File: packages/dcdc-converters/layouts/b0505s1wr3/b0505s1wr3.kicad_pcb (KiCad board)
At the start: 2 copper layers, 7 parts

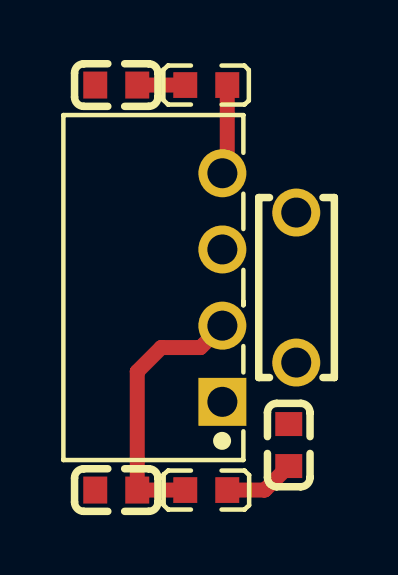
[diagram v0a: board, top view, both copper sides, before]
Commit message: Convert B0505 into ato
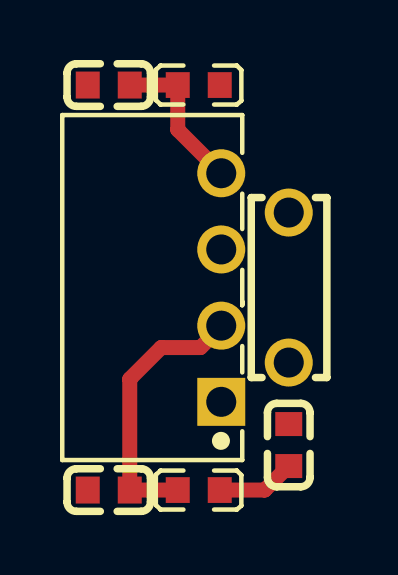
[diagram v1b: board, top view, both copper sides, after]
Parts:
- C2, C3: value 4.7µF ±10% 10V X5R -> 4.7nF ±10% 50V X7R
- moved C2 6.18 mm to (-1.50, 6.75), turned to 180 degrees
- moved C3 5.94 mm to (4.50, 5.25), turned to 90 degrees
- moved C1 0.25 mm to (4.50, 0.00)
- moved C4 0.25 mm to (-1.50, -6.75)
- moved L1 0.25 mm to (1.50, 6.75), turned to 0 degrees
- moved L2 0.25 mm to (1.50, -6.75)
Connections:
- C2 pad 1: hv -> plusVin
- C3 pad 1: hv-2 -> hv-1
- C4 pad 1: hv-1 -> plusVout
- L1 pad 1: hv -> plusVin
- L1 pad 2: hv-2 -> hv-1
- L2 pad 1: hv-1 -> plusVout
- L2 pad 2: hv-3 -> hv
- U1 pad 2: hv-2 -> plusVin
- U1 pad 4: hv-3 -> plusVout
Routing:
- net plusVin: track 0.00 -> 9.12 mm
- net hv-2: track 9.02 -> 0.00 mm
- net plusVout: track 0.00 -> 5.14 mm
- net hv-3: track 3.01 -> 0.00 mm
- net hv: track 2.38 -> 0.00 mm
- net hv-1: track 1.60 -> 2.63 mm

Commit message: Rebuild all
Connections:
- C3 pad 1: hv-1 -> hv
- L1 pad 2: hv-1 -> hv
- L2 pad 2: hv -> hv-1
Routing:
- net hv-1: track 2.63 -> 0.00 mm
- net hv: track 0.00 -> 2.63 mm
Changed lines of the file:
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@@
     )
     (net 0 "")
-    (net 1 "hv")
+    (net 1 "hv-1")
     (net 2 "plusVout")
     (net 3 "plusVin")
-    (net 4 "hv-1")
+    (net 4 "hv")
     (net 5 "gnd")
     (net 6 "gnd-1")
@@
             (size 0.8 0.86)
             (layers "F.Cu" "F.Mask" "F.Paste")
-            (net 4 "hv-1")
+            (net 4 "hv")
         )
         (embedded_fonts no)
@@
             (size 0.8 0.86)
             (layers "F.Cu" "F.Mask" "F.Paste")
-            (net 1 "hv")
+            (net 1 "hv-1")
         )
         (embedded_fonts no)
@@
             (size 0.8 0.9)
             (layers "F.Cu" "F.Mask" "F.Paste")
-            (net 4 "hv-1")
+            (net 4 "hv")
         )
         (pad "2" smd rect

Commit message: Update packages to ato v0.9.x (#36)
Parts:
- C1: footprint atopile:CAP-TH_L6.0-W2.5-P5.00-D1.0-5e41da -> STE_R06B1B271KN0B0S0N0:CAP-TH_L6.0-W2.5-P5.00-D1.0
- C2, C3: footprint atopile:C0603-bd72f6 -> FH_0603B472K500NT:C0603
- C4: footprint atopile:C0603-bd72f6 -> Samsung_Electro_Mechanics_CL10A106KP8NNNC:C0603
- L1, L2: footprint atopile:L0603-9cac2b -> FH_CMH160808B4R7MT:L0603
- U1: footprint atopile:PWRM-TH_B0505S-1WR3-83f76b -> EVISUN_B0505S_1WR3:PWRM-TH_B0505S-1WR3
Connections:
- net plusVin renamed Vinpos
- net plusVout renamed Voutpos
